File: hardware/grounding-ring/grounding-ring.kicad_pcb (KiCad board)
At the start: 2 copper layers, 28 x 38.2 mm, 1 part, among them P1 CONN_01X02

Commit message: grounding ring prototype
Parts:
- P1: footprint kicad-libraries:JST-PH-2 -> kicad-libraries:JST-PH-2-SMD
- moved P1 7.00 mm to (150.0, 117.0), turned to 180 degrees
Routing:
- net GND: vias 1 -> 58
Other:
- board size 28 x 38.2 mm -> 28.1 x 36.3 mm
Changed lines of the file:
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@@
     (thickness 1.6)
     (drawings 8)
-    (tracks 1)
+    (tracks 58)
     (zones 0)
     (modules 1)
@@
       (drillshape 0)
       (scaleselection 1)
-      (outputdirectory "../../../Schreibtisch/proto/breakout_V2/"))
+      (outputdirectory "../../../../Schreibtisch/proto/grounding-ring/"))
   )
   (net 0 "")
@@
     (add_net GND)
   )
-  (module kicad-libraries:JST-PH-2 (layer F.Cu)
-    (at 150 124)
-    (fp_text reference P1 (at 0 0) (layer F.Fab)
-      (effects (font (size 0.3 0.3) (thickness 0.075)))
+  (module kicad-libraries:JST-PH-2-SMD (layer F.Cu)
+    (at 150 117 180)
+    (fp_text reference P1 (at 0.09 -3.53) (layer F.Fab)
+      (effects (font (size 0.8 0.8) (thickness 0.15)))
     )
-    (fp_text value CONN_01X02 (at 0 0) (layer F.Fab)
-      (effects (font (size 0.3 0.3) (thickness 0.075)))
+    (fp_text value CONN_01X02 (at 0.48 -0.73) (layer F.Fab)
+      (effects (font (size 0.8 0.8) (thickness 0.15)))
     )
-    (fp_line (start -2.7 0) (end -2.1 -1.2) (layer F.Fab) (width 0.381))
-    (fp_line (start -2.1 -1.2) (end -1.6 0) (layer F.Fab) (width 0.381))
-    (fp_line (start 3.9 0) (end -3.9 0) (layer F.Fab) (width 0.381))
-    (fp_line (start -3.9 0) (end -3.9 -6) (layer F.Fab) (width 0.381))
-    (fp_line (start -3.9 -6) (end 3.9 -6) (layer F.Fab) (width 0.381))
-    (fp_line (start 3.9 -6) (end 3.9 0) (layer F.Fab) (width 0.381))
-    (pad 2 smd rect (at 1 -7.25) (size 1 3.5) (layers F.Cu F.Paste F.Mask)
+    (fp_line (start -3.975 -4.75) (end 3.975 -4.75) (layer F.Fab) (width 0.2))
+    (fp_line (start 3.975 -4.75) (end 3.975 0.25) (layer F.Fab) (width 0.2))
+    (fp_line (start 3.975 0.25) (end -3.975 0.25) (layer F.Fab) (width 0.2))
+    (fp_line (start -3.975 0.25) (end -3.975 -4.75) (layer F.Fab) (width 0.2))
+    (pad "" smd rect (at 3.4 -2.25 180) (size 1.6 3) (layers F.Paste F.Mask))
+    (pad "" smd rect (at -3.4 -2.25 180) (size 1.6 3) (layers F.Paste F.Mask))
+    (pad 2 smd rect (at 1 0 180) (size 1 5.5) (layers F.Cu F.Paste F.Mask)
       (net 1 GND))
-    (pad 1 smd rect (at -1 -7.25) (size 1 3.5) (layers F.Cu F.Paste F.Mask)
+    (pad 1 smd rect (at -1 0 180) (size 1 5.5) (layers F.Cu F.Paste F.Mask)
       (net 1 GND))
-    (pad EP smd rect (at 3.35 -1.7) (size 1.5 3.4) (layers F.Cu F.Paste F.Mask))
-    (pad EP smd rect (at -3.35 -1.7) (size 1.5 3.4) (layers F.Cu F.Paste F.Mask))
+    (model "../3d/Connectors/B2B-PH-SM4-TB(LF)(SN).wrl"
+      (at (xyz 0 0 0))
+      (scale (xyz 1 1 1))
+      (rotate (xyz 0 0 0))
+    )
   )
   (gr_poly (pts (xy 164 113) (xy 136 113) (xy 136 86) (xy 164 86)) (layer B.Mask) (width 0.1))
   (gr_poly (pts (xy 164 113) (xy 136 113) (xy 136 86) (xy 164 86)) (layer F.Mask) (width 0.1))
-  (gr_arc (start 150 100) (end 154.999999 113.099999) (angle -318.2183505) (layer Edge.Cuts) (width 0.1))
-  (gr_line (start 145 124.2) (end 145 113.1) (layer Edge.Cuts) (width 0.1))
-  (gr_line (start 155 124.2) (end 145 124.2) (layer Edge.Cuts) (width 0.1))
-  (gr_line (start 155 124.2) (end 155 113.1) (layer Edge.Cuts) (width 0.1))
+  (gr_arc (start 150 100) (end 155.1 113.099999) (angle -317.4567807) (layer Edge.Cuts) (width 0.1))
+  (gr_line (start 144.9 122.2) (end 144.9 113.1) (layer Edge.Cuts) (width 0.1))
+  (gr_line (start 155.1 122.2) (end 144.9 122.2) (layer Edge.Cuts) (width 0.1))
+  (gr_line (start 155.1 122.2) (end 155.1 113.1) (layer Edge.Cuts) (width 0.1))
   (gr_circle (center 150 100) (end 159.5 100) (layer Edge.Cuts) (width 0.1))
   (gr_text "Copyright Tinkerforge GmbH 2020.\nThis documentation describes Open Hardware and is licensed under the\nCERN OHL v. 1.1.\nYou may redistribute and modify this documentation under the terms of the\nCERN OHL v.1.1. (http://ohwr.org/cernohl). This documentation is distributed\nWITHOUT ANY EXPRESS OR IMPLIED WARRANTY, INCLUDING OF\nMERCHANTABILITY, SATISFACTORY QUALITY AND FITNESS FOR A\nPARTICULAR PURPOSE. Please see the CERN OHL v.1.1 for applicable\nconditions\n" (at 58.6 184.4) (layer F.Fab)
     (effects (font (size 1.5 1.5) (thickness 0.3)))
   )
-  (via (at 150 113) (size 0.55) (drill 0.25) (layers F.Cu B.Cu) (net 1))
+  (via (at 154.6 118.3) (size 0.55) (drill 0.25) (layers F.Cu B.Cu) (net 1))
+  (via (at 154.6 117.3) (size 0.55) (drill 0.25) (layers F.Cu B.Cu) (net 1))
+  (via (at 153.3 121.3) (size 0.55) (drill 0.25) (layers F.Cu B.Cu) (net 1))
+  (via (at 154.6 121.3) (size 0.55) (drill 0.25) (layers F.Cu B.Cu) (net 1))
+  (via (at 152.1 117.3) (size 0.55) (drill 0.25) (layers F.Cu B.Cu) (net 1))
+  (via (at 152.1 120.3) (size 0.55) (drill 0.25) (layers F.Cu B.Cu) (net 1))
+  (via (at 152.1 121.3) (size 0.55) (drill 0.25) (layers F.Cu B.Cu) (net 1))
+  (via (at 152.1 119.3) (size 0.55) (drill 0.25) (layers F.Cu B.Cu) (net 1))
+  (via (at 154.6 119.3) (size 0.55) (drill 0.25) (layers F.Cu B.Cu) (net 1))
+  (via (at 152.1 118.3) (size 0.55) (drill 0.25) (layers F.Cu B.Cu) (net 1))
+  (via (at 153.3 117.3) (size 0.55) (drill 0.25) (layers F.Cu B.Cu) (net 1))
+  (via (at 154.6 120.3) (size 0.55) (drill 0.25) (layers F.Cu B.Cu) (net 1))
+  (via (at 150 113.6) (size 0.55) (drill 0.25) (layers F.Cu B.Cu) (net 1))
+  (via (at 145.4 119.3) (size 0.55) (drill 0.25) (layers F.Cu B.Cu) (net 1))
+  (via (at 145.4 118.3) (size 0.55) (drill 0.25) (layers F.Cu B.Cu) (net 1))
+  (via (at 145.4 120.3) (size 0.55) (drill 0.25) (layers F.Cu B.Cu) (net 1))
+  (via (at 145.4 117.3) (size 0.55) (drill 0.25) (layers F.Cu B.Cu) (net 1))
+  (via (at 146.6 117.3) (size 0.55) (drill 0.25) (layers F.Cu B.Cu) (net 1))
+  (via (at 147.9 117.3) (size 0.55) (drill 0.25) (layers F.Cu B.Cu) (net 1))
+  (via (at 147.9 118.3) (size 0.55) (drill 0.25) (layers F.Cu B.Cu) (net 1))
+  (via (at 147.9 119.3) (size 0.55) (drill 0.25) (layers F.Cu B.Cu) (net 1))
+  (via (at 147.9 120.3) (size 0.55) (drill 0.25) (layers F.Cu B.Cu) (net 1))
+  (via (at 147.9 121.3) (size 0.55) (drill 0.25) (layers F.Cu B.Cu) (net 1))
+  (via (at 146.6 121.3) (size 0.55) (drill 0.25) (layers F.Cu B.Cu) (net 1))
+  (via (at 145.4 121.3) (size 0.55) (drill 0.25) (layers F.Cu B.Cu) (net 1))
+  (via (at 150 115) (size 0.55) (drill 0.25) (layers F.Cu B.Cu) (net 1))
+  (via (at 150 116.2) (size 0.55) (drill 0.25) (layers F.Cu B.Cu) (net 1))
+  (via (at 150 117.3) (size 0.55) (drill 0.25) (layers F.Cu B.Cu) (net 1))
+  (via (at 150 118.3) (size 0.55) (drill 0.25) (layers F.Cu B.Cu) (net 1))
+  (via (at 150 119.3) (size 0.55) (drill 0.25) (layers F.Cu B.Cu) (net 1))
+  (via (at 150 120.3) (size 0.55) (drill 0.25) (layers F.Cu B.Cu) (net 1))
+  (via (at 150 121.3) (size 0.55) (drill 0.25) (layers F.Cu B.Cu) (net 1))
+  (via (at 149 120.3) (size 0.55) (drill 0.25) (layers F.Cu B.Cu) (net 1))
+  (via (at 151 120.3) (size 0.55) (drill 0.25) (layers F.Cu B.Cu) (net 1))
+  (via (at 149 113.6) (size 0.55) (drill 0.25) (layers F.Cu B.Cu) (net 1))
+  (via (at 151 113.6) (size 0.55) (drill 0.25) (layers F.Cu B.Cu) (net 1))
+  (via (at 152.1 116.2) (size 0.55) (drill 0.25) (layers F.Cu B.Cu) (net 1))
+  (via (at 152.1 115.1) (size 0.55) (drill 0.25) (layers F.Cu B.Cu) (net 1))
+  (via (at 152.1 114.1) (size 0.55) (drill 0.25) (layers F.Cu B.Cu) (net 1))
+  (via (at 147.9 114.1) (size 0.55) (drill 0.25) (layers F.Cu B.Cu) (net 1))
+  (via (at 147.9 116.2) (size 0.55) (drill 0.25) (layers F.Cu B.Cu) (net 1))
+  (via (at 147.9 115.1) (size 0.55) (drill 0.25) (layers F.Cu B.Cu) (net 1))
+  (via (at 136.5 100) (size 0.55) (drill 0.25) (layers F.Cu B.Cu) (net 1))
+  (via (at 140 100) (size 0.55) (drill 0.25) (layers F.Cu B.Cu) (net 1))
+  (via (at 160 100) (size 0.55) (drill 0.25) (layers F.Cu B.Cu) (net 1))
+  (via (at 163.5 100) (size 0.55) (drill 0.25) (layers F.Cu B.Cu) (net 1))
+  (via (at 150 90) (size 0.55) (drill 0.25) (layers F.Cu B.Cu) (net 1))
+  (via (at 150 86.5) (size 0.55) (drill 0.25) (layers F.Cu B.Cu) (net 1))
+  (via (at 150 110) (size 0.55) (drill 0.25) (layers F.Cu B.Cu) (net 1))
+  (via (at 150 112.5) (size 0.55) (drill 0.25) (layers F.Cu B.Cu) (net 1))
+  (via (at 142.75 107.25) (size 0.55) (drill 0.25) (layers F.Cu B.Cu) (net 1))
+  (via (at 140.5 109.5) (size 0.55) (drill 0.25) (layers F.Cu B.Cu) (net 1))
+  (via (at 157.25 107.25) (size 0.55) (drill 0.25) (layers F.Cu B.Cu) (net 1))
+  (via (at 159.5 109.5) (size 0.55) (drill 0.25) (layers F.Cu B.Cu) (net 1))
+  (via (at 142.75 92.75) (size 0.55) (drill 0.25) (layers F.Cu B.Cu) (net 1))
+  (via (at 140.5 90.5) (size 0.55) (drill 0.25) (layers F.Cu B.Cu) (net 1))
+  (via (at 157.25 92.75) (size 0.55) (drill 0.25) (layers F.Cu B.Cu) (net 1))
+  (via (at 159.5 90.5) (size 0.55) (drill 0.25) (layers F.Cu B.Cu) (net 1))
   (zone (net 1) (net_name GND) (layer F.Cu) (hatch edge 0.508)
-    (connect_pads (clearance 0.2))
+    (connect_pads yes (clearance 0.2))
     (min_thickness 0.254)
     (fill yes (arc_segments 32) (thermal_gap 0.508) (thermal_bridge_width 0.508))

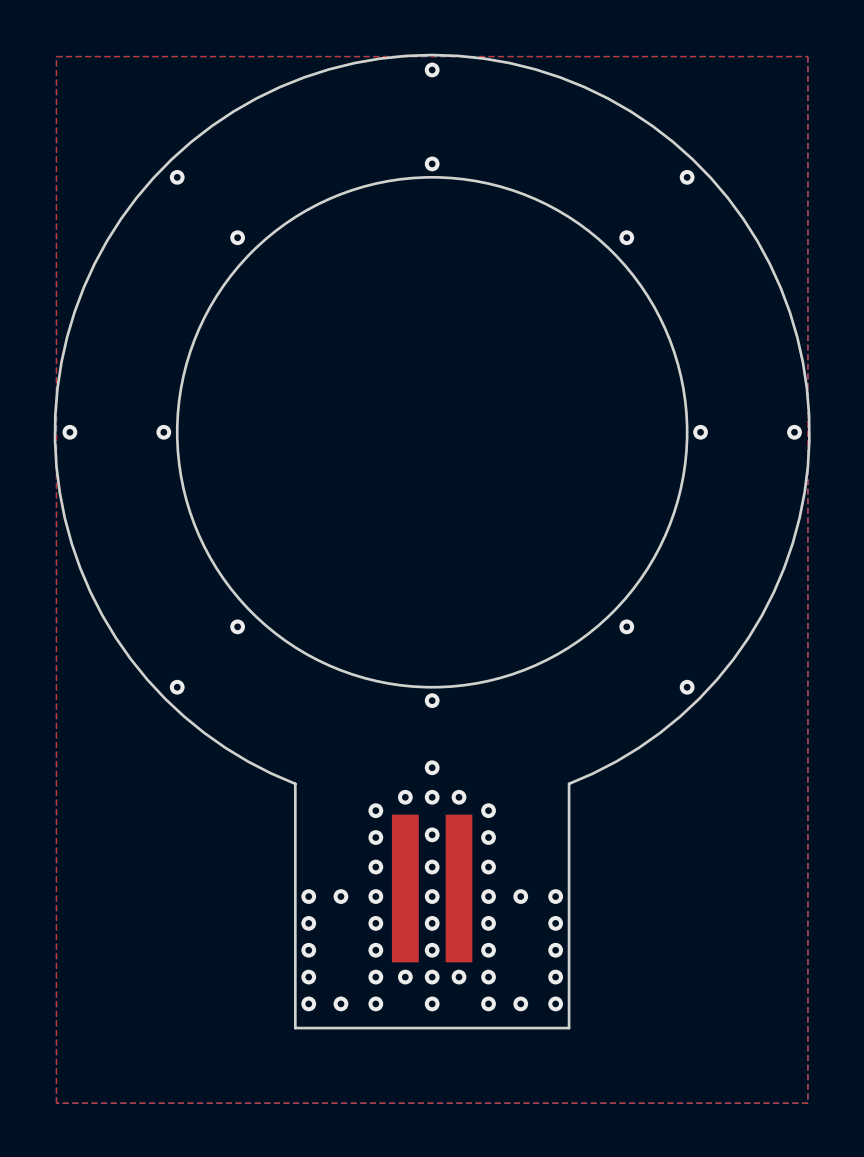
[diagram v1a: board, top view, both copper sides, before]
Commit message: changed groundingring layout
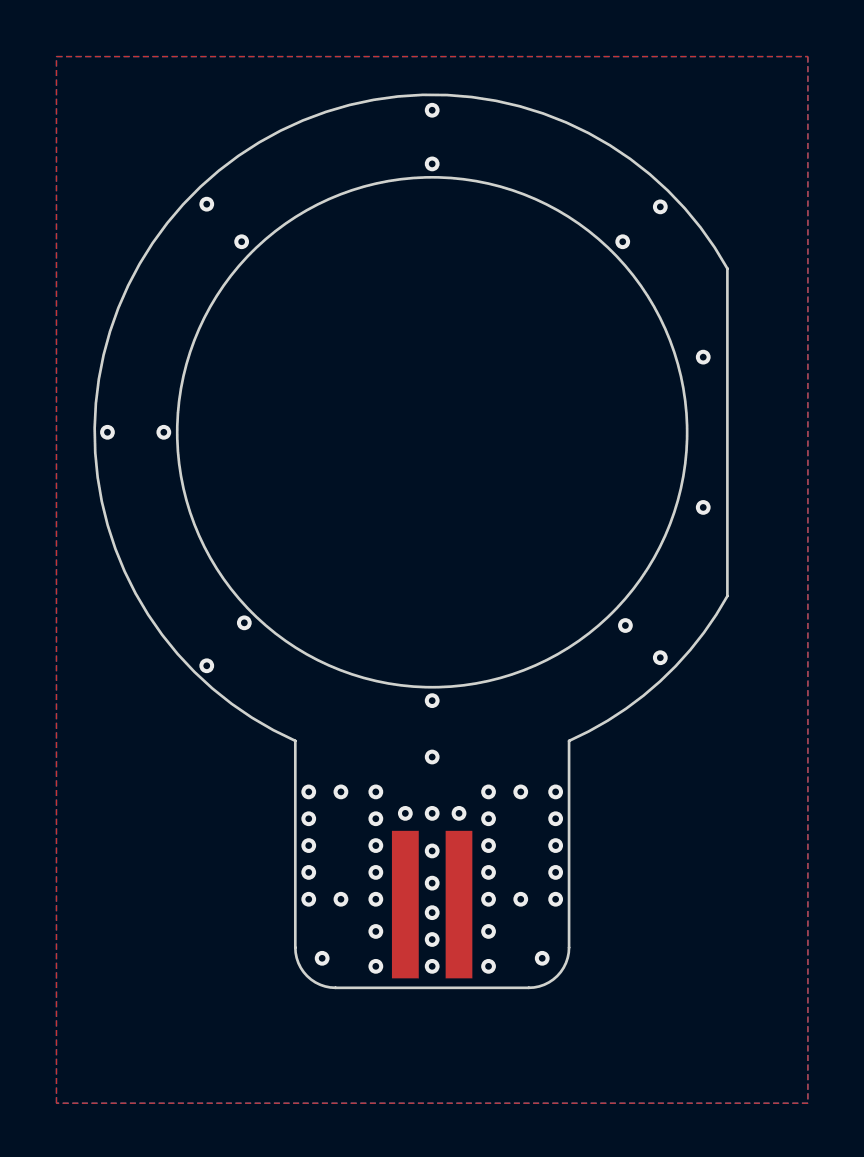
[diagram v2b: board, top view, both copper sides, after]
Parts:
- moved P1 0.60 mm to (150.0, 117.6), turned to 0 degrees
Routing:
- net GND: vias 58 -> 54
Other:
- board size 28.1 x 36.3 mm -> 23.6 x 33.3 mm
